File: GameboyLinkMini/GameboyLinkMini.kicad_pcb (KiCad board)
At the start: 2 copper layers, 29.5 x 41.5 mm, 14 parts, among them J2 AVR-ISP-6, SW1 SW_Reset, U1 ATtiny2313-20S, U2 DS1307Z+, Y1 Crystal

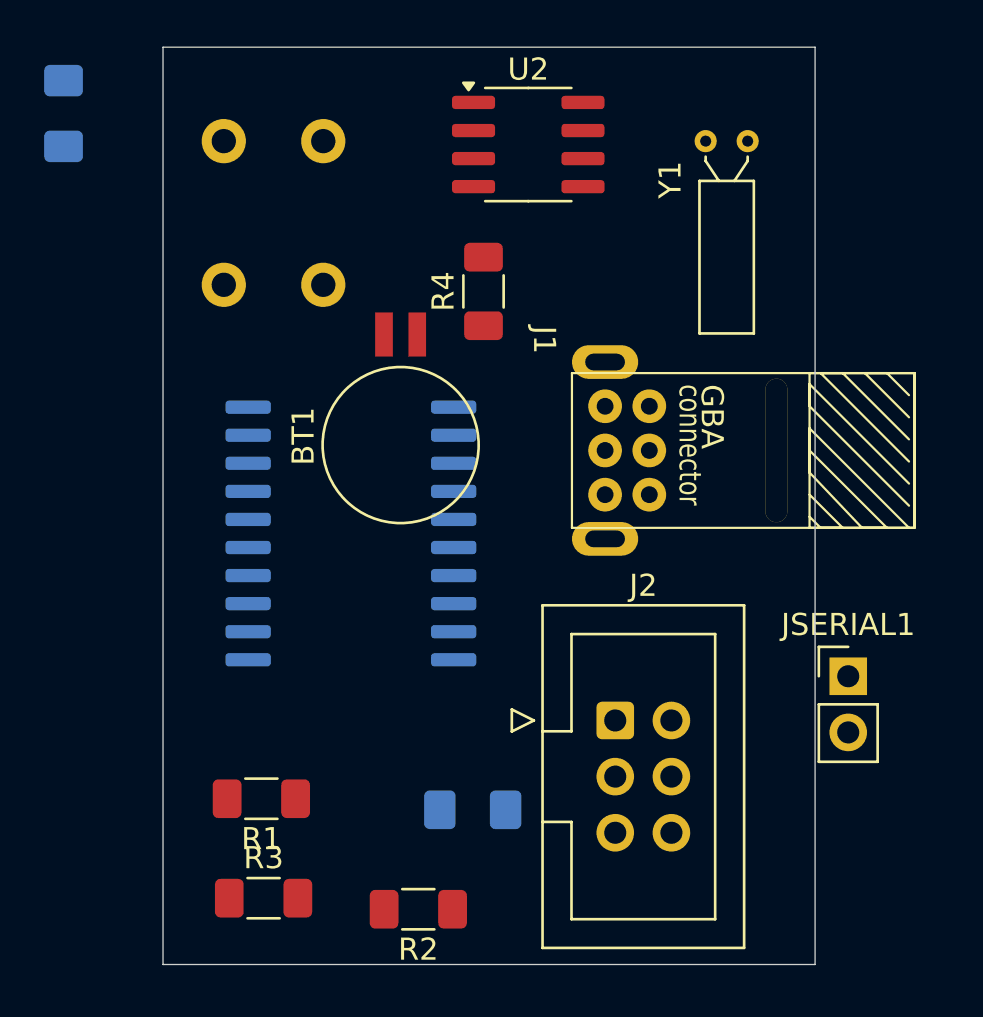
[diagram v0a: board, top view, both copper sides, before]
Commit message: Schematic and first version of PCB ready
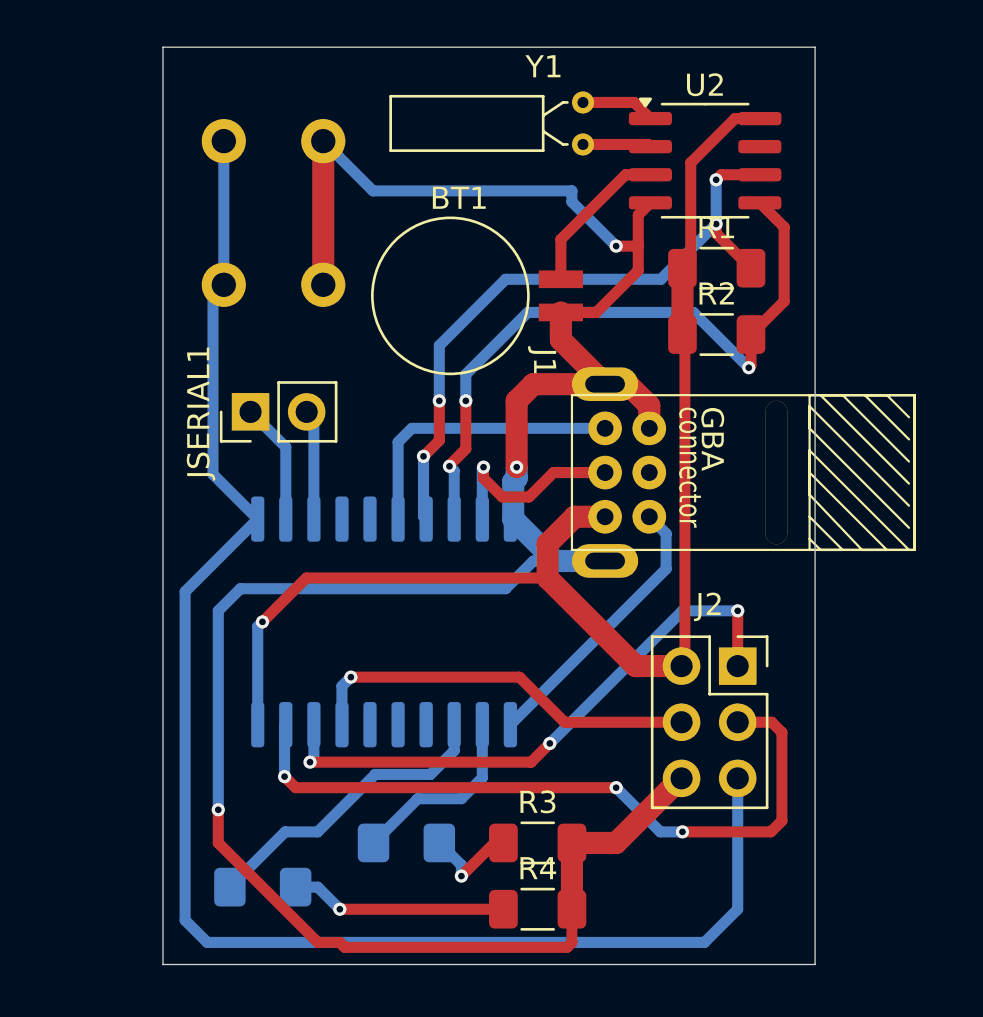
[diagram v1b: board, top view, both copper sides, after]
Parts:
- J2: footprint Connector_IDC:IDC-Header_2x03_P2.54mm_Vertical -> Connector_PinSocket_2.54mm:PinSocket_2x03_P2.54mm_Vertical
- moved D2 36.1 mm to (175.0, 107.0), turned to 180 degrees
- moved R1 31.6 mm to (195.6, 79.0), turned to 0 degrees
- moved JSERIAL1 29.6 mm to (174.5, 85.5), turned to 90 degrees
- moved R2 29.3 mm to (195.6, 82.0), turned to 0 degrees
- moved R4 28.1 mm to (187.4, 108.0), turned to 0 degrees
- moved R3 12.6 mm to (187.4, 105.0)
- moved U2 8.03 mm to (195.0, 74.1)
- moved BT1 7.46 mm to (188.5, 80.2), turned to 0 degrees
- moved J2 6.06 mm to (196.5, 97.0)
- moved Y1 5.82 mm to (189.5, 71.5), turned to -90 degrees
- moved U1 4.27 mm to (180.5, 95.0), turned to -90 degrees
- moved D1 3.35 mm to (181.5, 105.0), turned to 180 degrees
- moved J1 1.00 mm to (187.2, 83.2)
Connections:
- Y1 pad 1: Net-(U2-X2) -> Net-(U2-X1)
- Y1 pad 2: Net-(U2-X1) -> Net-(U2-X2)
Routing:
- net /GND: track 0.00 -> 110.4 mm, vias 0 -> 3
- net /~RESET: track 0.00 -> 69.6 mm
- net /VCC: track 0.00 -> 57.8 mm, vias 0 -> 1
- net /SCK: track 0.00 -> 32.3 mm, vias 0 -> 3
- net Net-(U1-PD4): track 0.00 -> 30.5 mm, vias 0 -> 3
- net Net-(U1-PD3): track 0.00 -> 29.7 mm, vias 0 -> 4
- net /MISO: track 0.00 -> 26.5 mm, vias 0 -> 3
- net /MOSI: track 0.00 -> 18.1 mm, vias 0 -> 1
- net /L2: track 0.00 -> 13.9 mm
- net /GB_CLK: track 0.00 -> 13.1 mm
- net /GB_OUT: track 0.00 -> 12.6 mm
- net Net-(D2-K): track 0.00 -> 9.81 mm, vias 0 -> 1
- net /GB_IN: track 0.00 -> 9.18 mm, vias 0 -> 1
- net /L1: track 0.00 -> 8.54 mm
- net Net-(BT1-+): track 0.00 -> 7.07 mm
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
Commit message: Sent to production (v1.0)
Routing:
- added copper zone on F.Cu, net /GND
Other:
- board text added: "1307"
- board text added: "GBClock (Mini)"
- board text added: "GameboyLink-Mini"
- board text added: "JLCJLCJLCJLC"
- board text added: "Reset"
- board text added: "Tiny2313"
- board text added: "electrogeek.cc"
- board text added: "v1.0 - June2024"
